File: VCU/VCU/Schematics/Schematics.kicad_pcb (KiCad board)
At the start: 2 copper layers, 25 parts, among them U1 ATSAMC21J18A-ANT, U2 ATA6561-GAQW-N, U3 ATA6561-GAQW-N

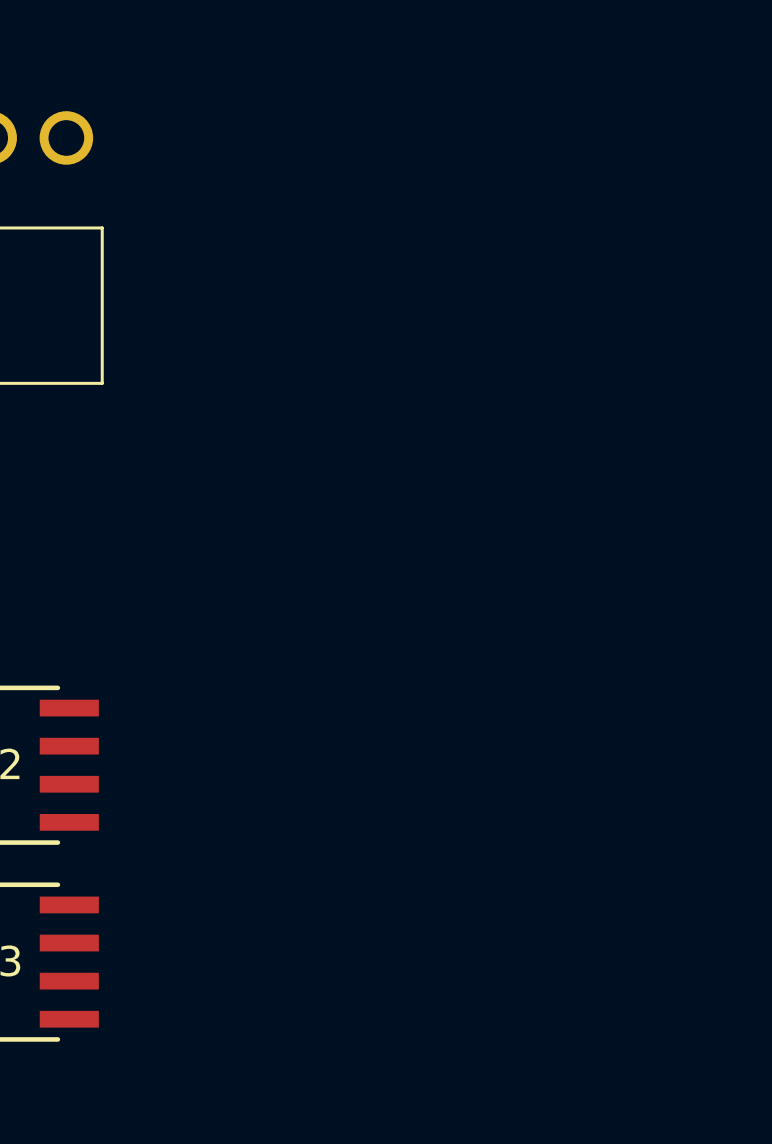
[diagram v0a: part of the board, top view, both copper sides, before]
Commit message: Update schematics VCU et ajout protocoles de tests
Ajout de protocoles de tests et ajout de l'interface microSD dans les schematics
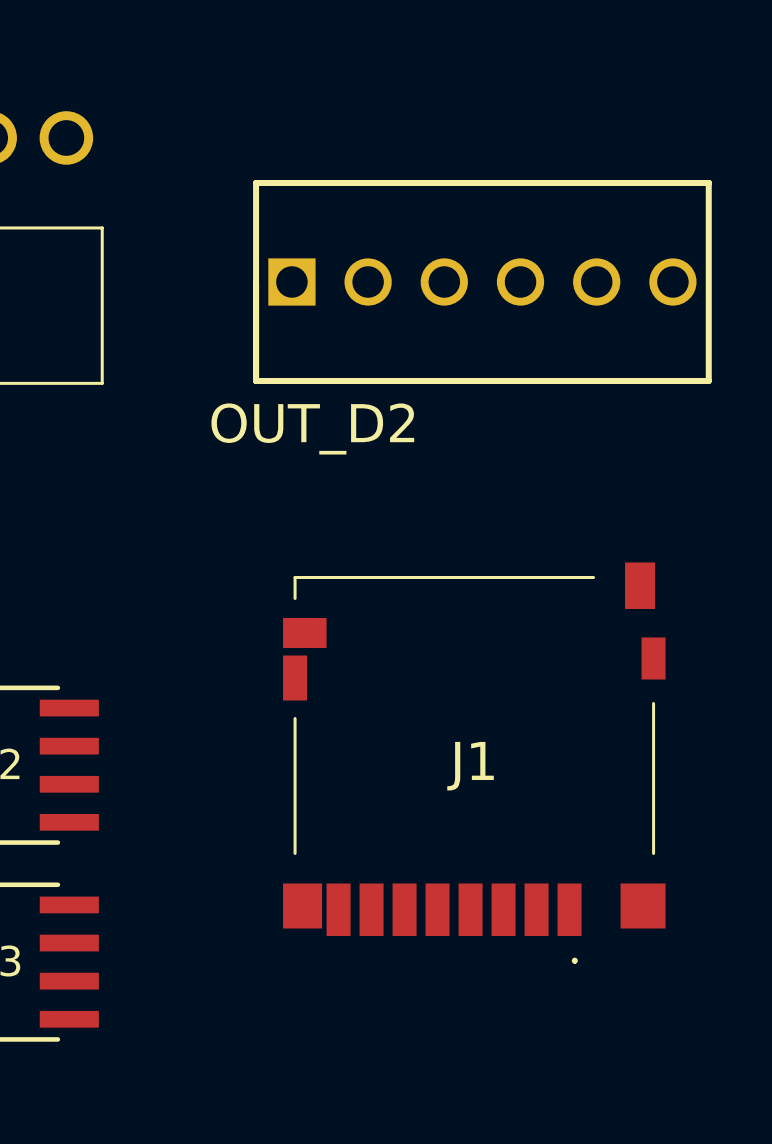
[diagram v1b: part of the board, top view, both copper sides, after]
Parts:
- added J1: DM3D-SF, ATSAMC21J18A-ANT:DM3DSF, F.Cu at (165.5, 106.5)
- added OUT_D2: 6P Droit 22-11-2062, EPSA_lib:HDRV6W87P0X254_1X6_1509X635X1092P, F.Cu at (159.4, 90.9)
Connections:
- C11 pad 2: VCC_CAN -> VDD_IO
- C12 pad 2: VCC_CAN -> VDD_IO
- C6 pad 2: VCC_CAN -> VDD_IO
- C7 pad 2: VCC_CAN -> VDD_IO
- C8 pad 2: VCC_CAN -> VDD_IO
- Debug/Prog1 pad 1: unconnected-(Debug/Prog1-Pad1) -> RESETN
- Debug/Prog1 pad 2: unconnected-(Debug/Prog1-Pad2) -> VDD_IO
- Debug/Prog1 pad 3: unconnected-(Debug/Prog1-Pad3) -> GND
- Debug/Prog1 pad 4: unconnected-(Debug/Prog1-Pad4) -> SWO
- Debug/Prog1 pad 5: unconnected-(Debug/Prog1-Pad5) -> SWDCLK
- Debug/Prog1 pad 8: unconnected-(Debug/Prog1-Pad8) -> SWDIO
- L1 pad 1: VCC_CAN -> VDD_IO
- PS1 pad 4: VCC_CAN -> VDD_IO
- U1 pad 34: VCC_CAN -> VDD_IO
- U1 pad 48: VCC_CAN -> VDD_IO
- U1 pad 52: unconnected-(U1-RESETN-Pad52) -> RESETN
- U1 pad 56: VCC_CAN -> VDD_IO
- U1 pad 57: unconnected-(U1-PA30-Pad57) -> SWDCLK
- U1 pad 58: unconnected-(U1-PA31-Pad58) -> SWDIO
- U2 pad 3: VCC_CAN -> VDD_IO
- U2 pad 5: VCC_CAN -> VDD_IO
- U3 pad 3: VCC_CAN -> VDD_IO
- U3 pad 5: VCC_CAN -> VDD_IO
